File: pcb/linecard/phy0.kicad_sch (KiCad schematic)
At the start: 32 parts, among them J6 XILINX_JTAG, J7 SMPM, J8 SMPM, U10 VSC8512, U60 SIT9121AC-2B2-33E125.000000

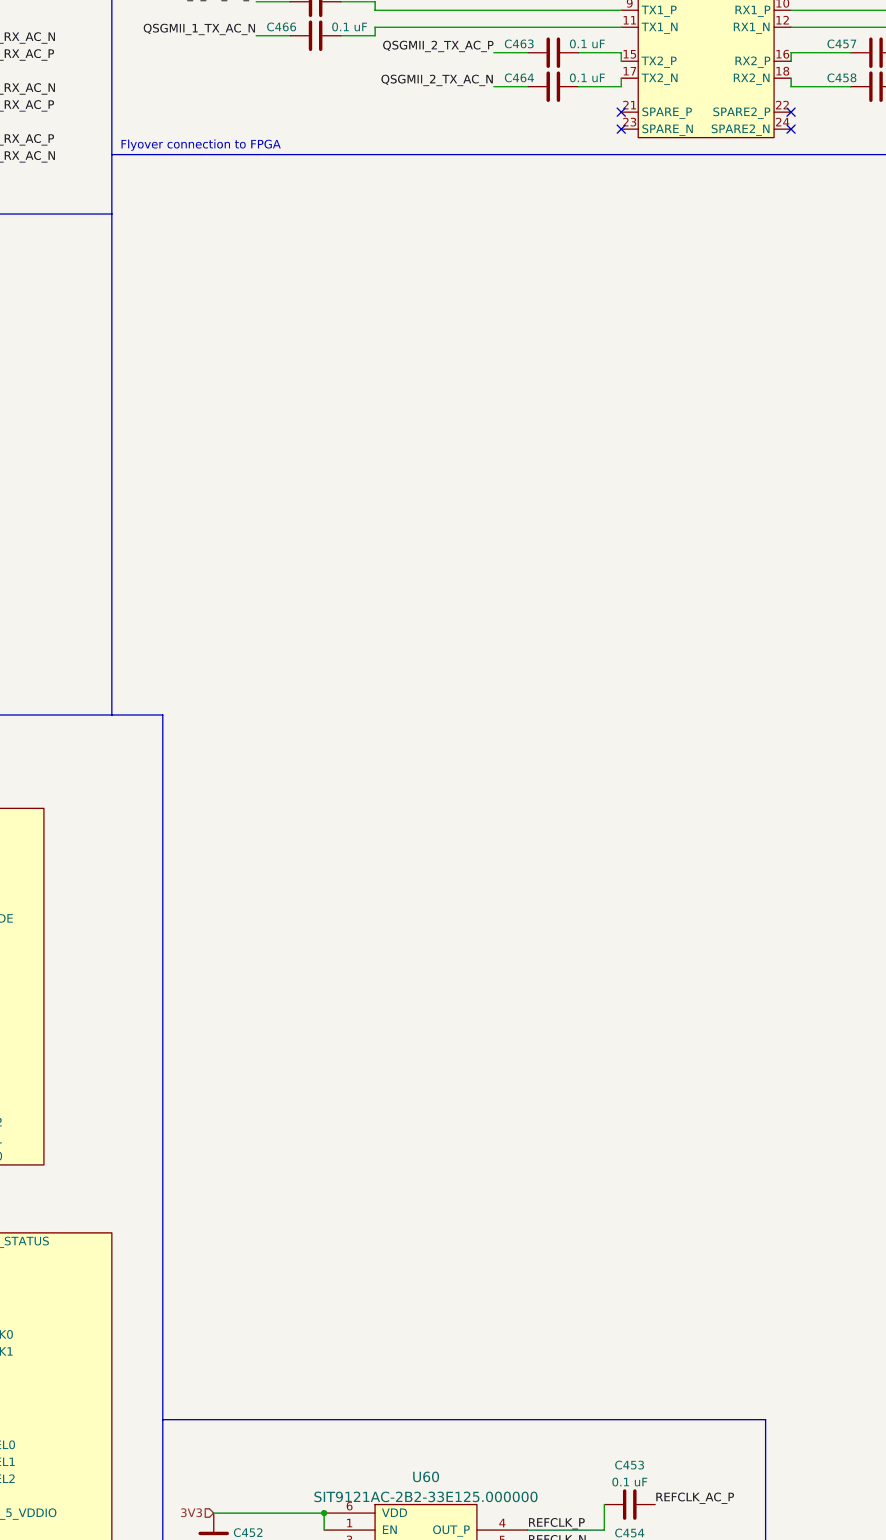
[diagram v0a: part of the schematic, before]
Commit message: Added heatsink, some silkscreen logos, mounting holes, and ground clips
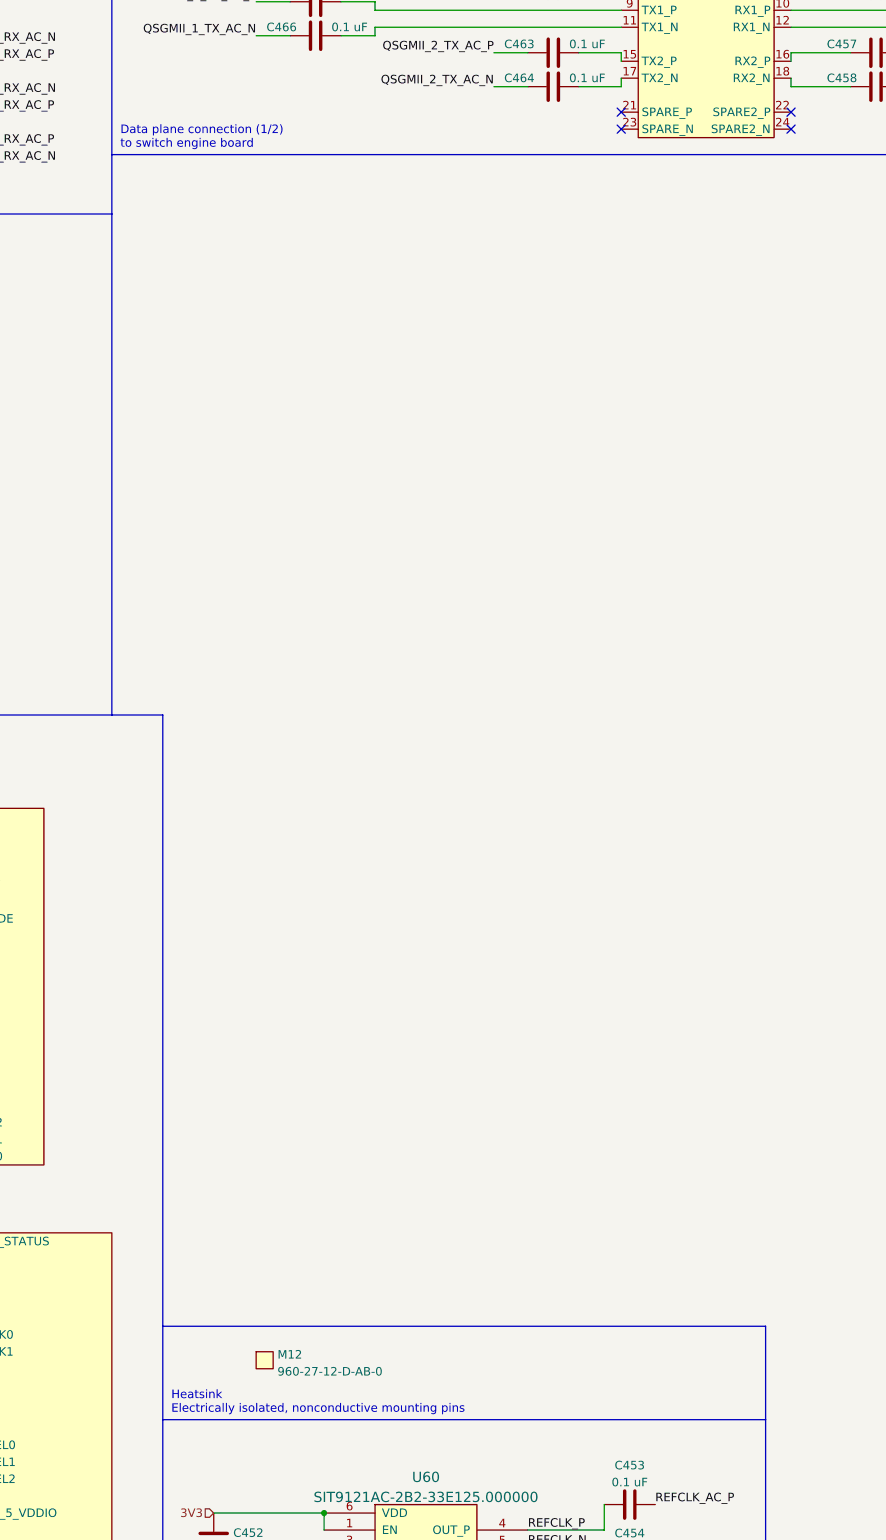
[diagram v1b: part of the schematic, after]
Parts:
- added M12: 960-27-12-D-AB-0, azonenberg_pcb:HEATSINK_WAKEFIELDVETTE_960-27-12-D-AB-0, symbol special-azonenberg:MECHANICAL
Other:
- note added: "Data plane connection (1/2) to switch engine board"
- note added: "Heatsink Electrically isolated, nonconductive mounting pins"
- note removed: "Flyover connection to FPGA"
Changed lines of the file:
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@@
 		)
 	)
+	(polyline
+		(pts
+			(xy 214.63 254) (xy 214.63 240.03)
+		)
+		(stroke
+			(width 0)
+			(type default)
+		)
+	)
 	(wire
 		(pts
@@
 		)
 	)
+	(polyline
+		(pts
+			(xy 214.63 240.03) (xy 124.46 240.03)
+		)
+		(stroke
+			(width 0)
+			(type default)
+		)
+	)
 	(wire
 		(pts
@@
 		)
 	)
+	(text "Heatsink\nElectrically isolated, nonconductive mounting pins"
+		(exclude_from_sim no)
+		(at 125.73 251.46 0)
+		(effects
+			(font
+				(size 1.27 1.27)
+			)
+			(justify left)
+		)
+	)
 	(text "QSGMII SERDES"
 		(exclude_from_sim no)
@@
 		)
 	)
-	(text "Flyover connection to FPGA"
+	(text "Data plane connection (1/2)\nto switch engine board"
 		(exclude_from_sim no)
-		(at 118.11 63.5 0)
+		(at 118.11 62.23 0)
 		(effects
 			(font
@@
 					(unit 1)
 				)
+			)
+		)
+	)
+	(symbol
+		(lib_id "special-azonenberg:MECHANICAL")
+		(at 138.43 245.11 0)
+		(unit 1)
+		(exclude_from_sim no)
+		(in_bom yes)
+		(on_board yes)
+		(dnp no)
+		(property "Reference" "M12"
+			(at 141.605 244.2753 0)
+			(effects
+				(font
+					(size 1.27 1.27)
+				)
+				(justify left)
+			)
+		)
+		(property "Value" "960-27-12-D-AB-0"
+			(at 141.605 246.8122 0)
+			(effects
+				(font
+					(size 1.27 1.27)
+				)
+				(justify left)
+			)
+		)
+		(property "Footprint" "azonenberg_pcb:HEATSINK_WAKEFIELDVETTE_960-27-12-D-AB-0"
+			(at 138.43 245.11 0)
+			(effects
+				(font
+					(size 1.27 1.27)
+				)
+				(hide yes)
+			)
+		)
+		(property "Datasheet" ""
+			(at 138.43 245.11 0)
+			(effects
+				(font
+					(size 1.27 1.27)
+				)
+				(hide yes)
+			)
+		)
+		(property "Description" ""
+			(at 138.43 245.11 0)
+			(effects
+				(font
+					(size 1.27 1.27)
+				)
+				(hide yes)
+			)
+		)
+		(instances
+			(project "linecard"
+				(path "/a55ad1ec-4cad-4d06-8b73-31c98dcc1d79/51c28a30-f923-4afc-abce-15dfcaf7ef81"
+					(reference "M12")
+					(unit 1)
+				)

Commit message: Finished initial schematic review
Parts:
- added TP23: TESTPOINT, symbol conn:CONN_01X01
- J10: value ~ -> ARF6-08-S-D-A-K-TR; footprint (none) -> azonenberg_pcb:CONN_SAMTEC_ARF6-08-S-D-A-K-TR
- R59: value 10K -> 1K
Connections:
- net GND: now also J10.27 (SHLD)
- net at U10.R2 (MDINT): now also TP23.1 (P1)
- no-connect marks 43 -> 42
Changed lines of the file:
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@@
 	(title_block
 		(title "LATENTRED Line Card")
-		(date "2024-12-10")
+		(date "2024-12-11")
 		(rev "0.1")
 		(company "Antikernel Labs")
@@
 	)
 	(junction
+		(at 193.04 20.32)
+		(diameter 0)
+		(color 0 0 0 0)
+	)
+	(junction
 		(at 218.44 22.86)
 		(diameter 0)
@@
 	)
 	(no_connect
-		(at 85.09 189.23)
-	)
-	(no_connect
 		(at 193.04 58.42)
 	)
@@
 	(wire
 		(pts
+			(xy 193.04 17.78) (xy 193.04 20.32)
+		)
+		(stroke
+			(width 0)
+			(type default)
+		)
+	)
+	(wire
+		(pts
 			(xy 39.37 167.64) (xy 39.37 170.18)
 		)
@@
 	(wire
 		(pts
+			(xy 72.39 189.23) (xy 85.09 189.23)
+		)
+		(stroke
+			(width 0)
+			(type default)
+		)
+	)
+	(wire
+		(pts
 			(xy 59.69 204.47) (xy 85.09 204.47)
 		)
@@
 	)
 	(label "GND"
-		(at 193.04 20.32 180)
+		(at 193.04 17.78 180)
 		(fields_autoplaced yes)
 		(effects
@@
 	)
 	(symbol
+		(lib_id "conn:CONN_01X01")
+		(at 67.31 189.23 180)
+		(unit 1)
+		(exclude_from_sim no)
+		(in_bom yes)
+		(on_board yes)
+		(dnp no)
+		(fields_autoplaced yes)
+		(property "Reference" "TP23"
+			(at 67.31 183.9425 0)
+			(effects
+				(font
+					(size 1.27 1.27)
+				)
+			)
+		)
+		(property "Value" "TESTPOINT"
+			(at 67.31 186.3668 0)
+			(effects
+				(font
+					(size 1.27 1.27)
+				)
+			)
+		)
+		(property "Footprint" ""
+			(at 67.31 189.23 0)
+			(effects
+				(font
+					(size 1.27 1.27)
+				)
+				(hide yes)
+			)
+		)
+		(property "Datasheet" ""
+			(at 67.31 189.23 0)
+			(effects
+				(font
+					(size 1.27 1.27)
+				)
+				(hide yes)
+			)
+		)
+		(property "Description" "Connector, single row, 01x01, pin header"
+			(at 67.31 189.23 0)
+			(effects
+				(font
+					(size 1.27 1.27)
+				)
+				(hide yes)
+			)
+		)
+		(pin "1"
+		)
+		(instances
+			(project ""
+				(path "/a55ad1ec-4cad-4d06-8b73-31c98dcc1d79/51c28a30-f923-4afc-abce-15dfcaf7ef81"
+					(reference "TP23")
+					(unit 1)
+				)
+			)
+		)
+	)
+	(symbol
 		(lib_id "device:C")
 		(at 231.14 54.61 90)
@@
 		(on_board yes)
 		(dnp no)
-		(fields_autoplaced yes)
 		(property "Reference" "J10"
-			(at 205.74 16.5185 0)
+			(at 205.74 13.335 0)
 			(effects
 				(font
@@
 			)
 		)
-		(property "Value" "~"
-			(at 205.74 18.1999 0)
+		(property "Value" "ARF6-08-S-D-A-K-TR"
+			(at 205.74 15.24 0)
 			(effects
 				(font
@@
 			)
 		)
-		(property "Footprint" ""
+		(property "Footprint" "azonenberg_pcb:CONN_SAMTEC_ARF6-08-S-D-A-K-TR"
 			(at 195.58 62.23 0)
 			(effects
@@
 		(pin "4"
 		)
+		(pin "27"
+		)
 		(instances
 			(project ""
@@
 			)
 		)
-		(property "Value" "10K"
+		(property "Value" "1K"
 			(at 67.31 173.99 90)
 			(effects

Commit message: Began layout of first few ports and left VSC8512
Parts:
- TP23: footprint (none) -> azonenberg_pcb:TESTPOINT_SMT_0.5MM
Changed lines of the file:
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@@
 			)
 		)
-		(property "Footprint" ""
+		(property "Footprint" "azonenberg_pcb:TESTPOINT_SMT_0.5MM"
 			(at 67.31 189.23 0)
 			(effects

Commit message: Left half getting close to finished
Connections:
- net REFCLK_AC_N: now also C453.2; no longer C454.2
- net REFCLK_AC_P: now also C454.2; no longer C453.2
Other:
- note added: "Invert polarity No need to correct Just a freq ref"
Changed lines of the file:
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@@
+		)
+	)
+	(text "Invert polarity\nNo need to correct\nJust a freq ref"
+		(exclude_from_sim no)
+		(at 173.99 280.67 0)
+		(effects
+			(font
+				(size 1.27 1.27)
+			)
+			(justify left)
 		)
 	)
@@
 	)
 	(label "REFCLK_AC_N"
-		(at 198.12 276.86 0)
+		(at 198.12 266.7 0)
 		(fields_autoplaced yes)
 		(effects
@@
 	)
 	(label "REFCLK_AC_P"
-		(at 198.12 266.7 0)
-		(fields_autoplaced yes)
-		(effects
+		(at 198.12 276.86 0)
+		(fields_autoplaced yes)
+		(effects

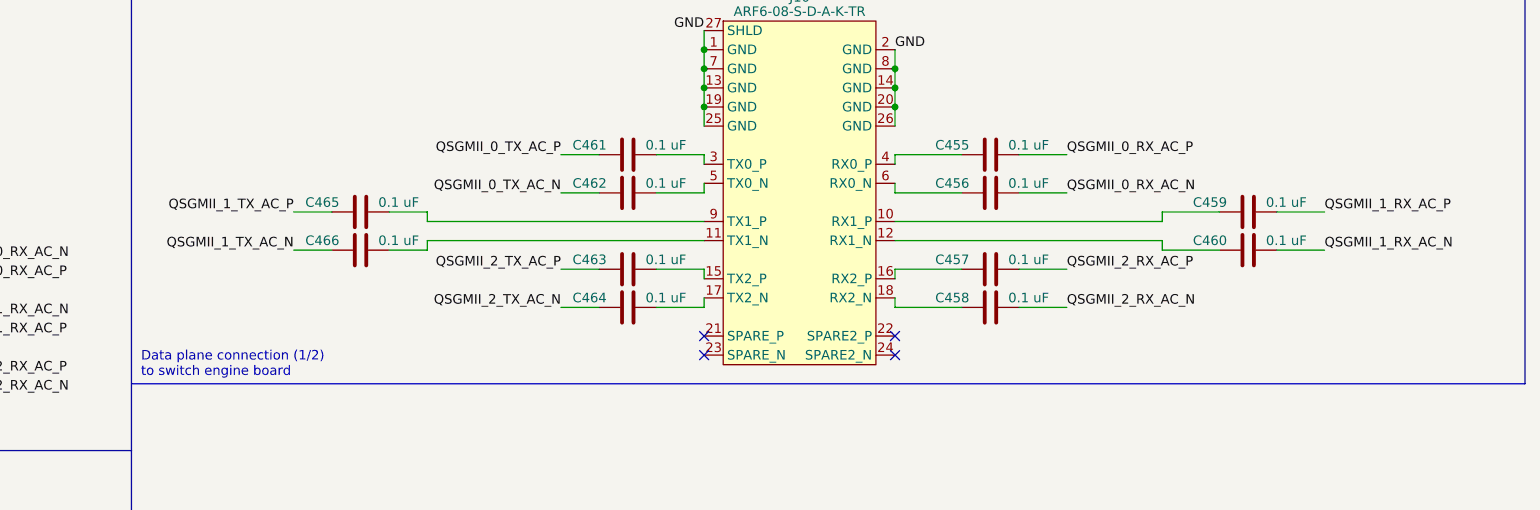
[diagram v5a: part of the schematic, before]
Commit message: Continued routing left PHY, put right PHY + heatsink in approximately final position
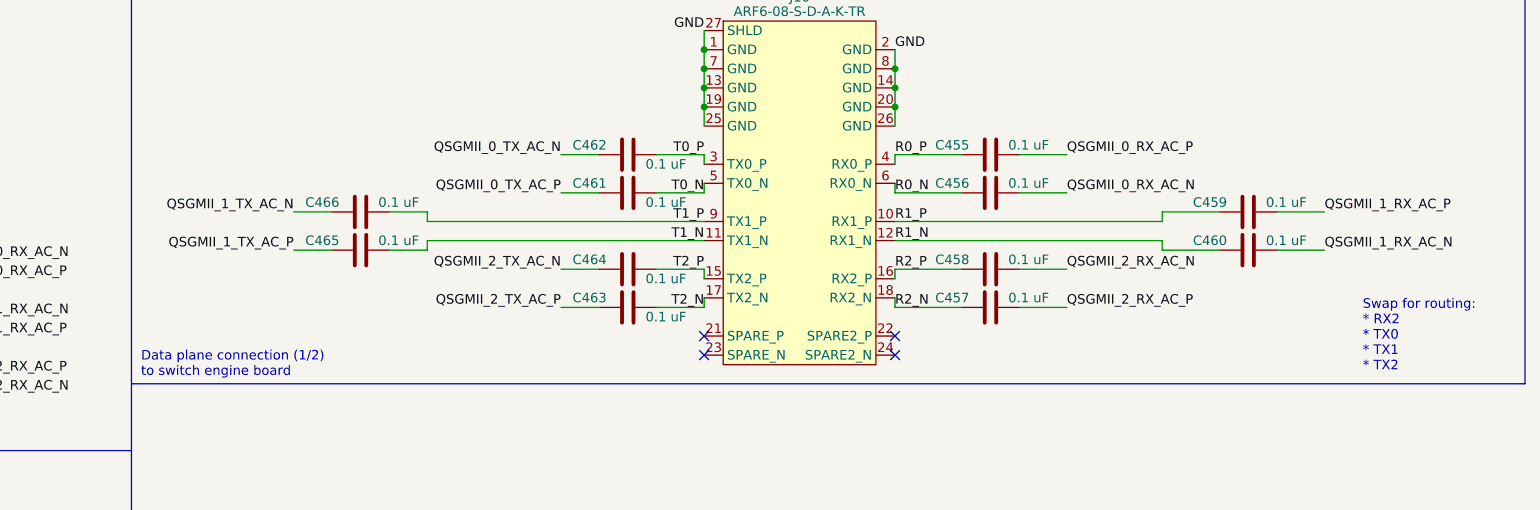
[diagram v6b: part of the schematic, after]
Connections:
- net T0_N: now reaches J10.5 (TX0_N)
- net T0_N: now also C461.2; no longer C462.2
- net T1_N: now reaches J10.11 (TX1_N)
- net T1_N: now also C465.2; no longer C466.2
- net R0_N: now reaches C456.1, J10.6 (RX0_N)
- net R2_N: now reaches J10.18 (RX2_N)
- net R2_N: now also C457.1; no longer C458.1
- net T2_N: now reaches C463.2
- net T2_N: now also J10.17 (TX2_N); no longer J10.15 (TX2_P)
- net R1_P: now reaches C459.1, J10.10 (RX1_P)
- net R1_N: now reaches C460.1, J10.12 (RX1_N)
- net R2_P: now reaches J10.16 (RX2_P)
- net R2_P: now also C458.1; no longer C457.1
- net T2_P: now reaches C464.2
- net T2_P: now also J10.15 (TX2_P); no longer J10.17 (TX2_N)
- net T0_P: now reaches J10.3 (TX0_P)
- net T0_P: now also C462.2; no longer C461.2
- net R0_P: now reaches C455.1, J10.4 (RX0_P)
- net T1_P: now reaches J10.9 (TX1_P)
- net T1_P: now also C466.2; no longer C465.2
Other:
- note added: "Swap for routing: * RX2 * TX0 * TX1 * TX2"
- moved on the sheet: C457, C458, C461, C462, C463, C464, C465, C466
